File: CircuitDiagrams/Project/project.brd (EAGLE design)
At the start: 100 x 70 mm, 124 parts, among them IC1 UC3C, IC2 PCA9542A, IC3 MT48LC4M16A2TSOP54, IC4 TB6593FNGSSOP20, IC5 TB6593FNGSSOP20, J1 JTAG2.54MM2X5TH, J2 1BY2THROUGHHOLE, J3 1BY2THROUGHHOLE, J4 1BY2THROUGHHOLE, J5 8PIN2.54MM2X4TH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

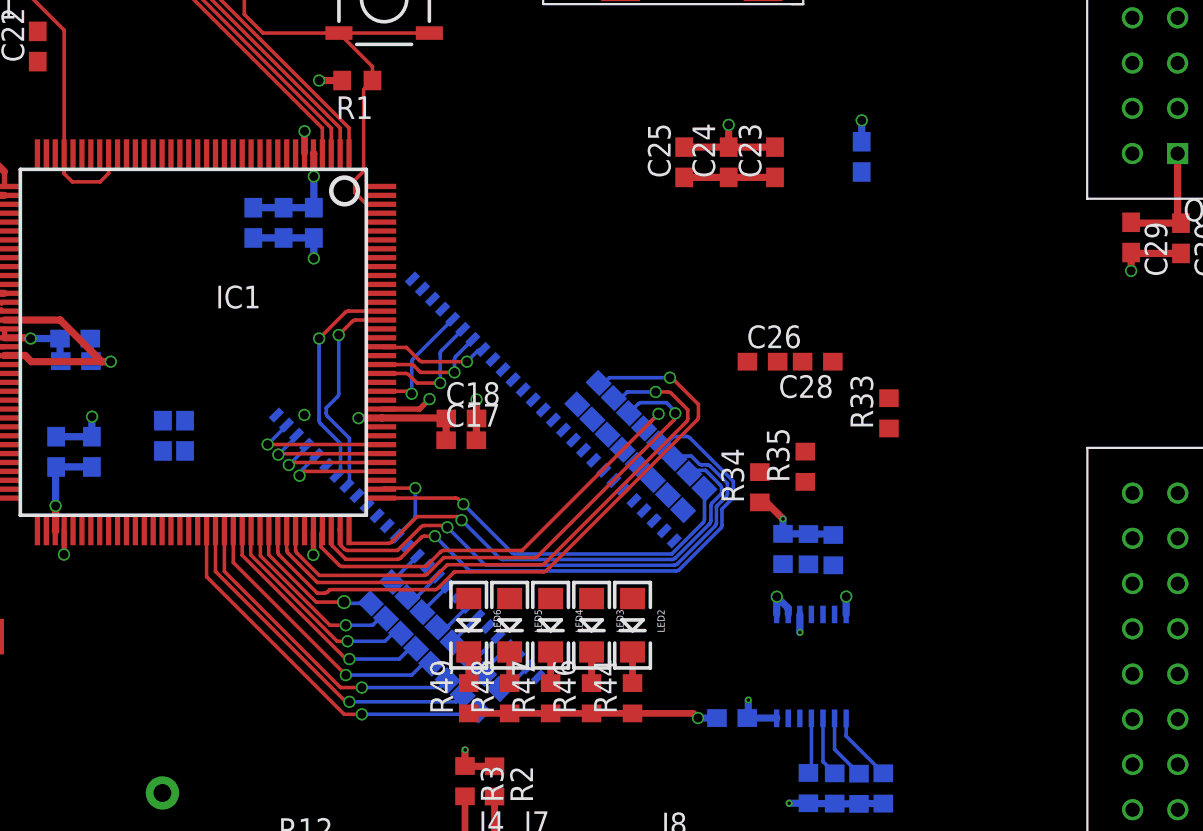
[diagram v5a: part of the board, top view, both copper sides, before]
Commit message: Routed the SDRAM
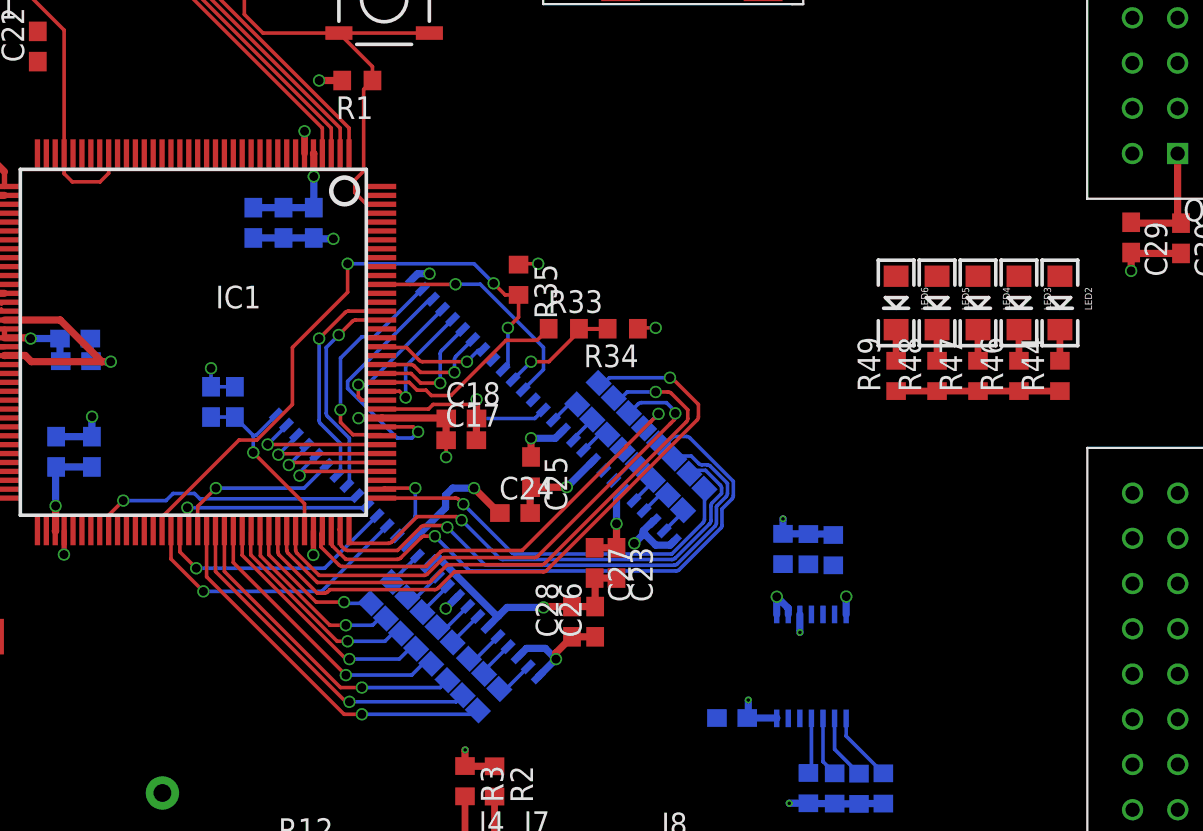
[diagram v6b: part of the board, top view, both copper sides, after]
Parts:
- moved LED2 30.1 mm to (90.4, 36.6)
- moved LED3 30.1 mm to (88.1, 36.6)
- moved LED4 30.1 mm to (85.8, 36.6)
- moved LED5 30.1 mm to (83.5, 36.6)
- moved LED6 30.1 mm to (81.2, 36.6)
- moved R44 30.1 mm to (90.4, 32.5)
- moved R46 30.1 mm to (88.1, 32.5)
- moved R47 30.1 mm to (85.8, 32.5)
- moved R48 30.1 mm to (83.5, 32.5)
- moved R49 30.1 mm to (81.2, 32.5)
- moved C27 27.3 mm to (64.3, 22.0), flipped to the top, turned to 270 degrees
- moved C23 24.2 mm to (65.5, 22.0), turned to 270 degrees
- moved C24 23.1 mm to (59.8, 24.8), turned to 0 degrees
- moved C28 20.1 mm to (63.0, 18.7), turned to 90 degrees
- moved C25 19.4 mm to (60.7, 27.1), turned to 270 degrees
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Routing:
- net PC14: track 0.00 -> 34.8 mm, vias 0 -> 3
- net +3V3: track 133.0 -> 162.5 mm, vias 23 -> 31
- net GND: track 157.5 -> 182.3 mm, vias 33 -> 34
- net PC15: track 0.00 -> 16.0 mm, vias 0 -> 1
- net PC8: track 0.00 -> 15.5 mm, vias 0 -> 1
- net PD10: track 0.00 -> 14.5 mm, vias 0 -> 1
- net PC16: track 0.00 -> 13.8 mm, vias 0 -> 1
- net PD24: track 0.00 -> 13.4 mm, vias 0 -> 1
- net PD9: track 0.00 -> 12.5 mm, vias 0 -> 1
- net PC17: track 0.00 -> 11.5 mm, vias 0 -> 1
- net PD13: track 0.00 -> 11.2 mm
- net PC18: track 0.00 -> 9.59 mm, vias 0 -> 1
- net PD11: track 0.00 -> 8.57 mm, vias 0 -> 1
- net SDRAMCLK: track 0.00 -> 8.11 mm, vias 0 -> 1
- net DQ08: track 0.00 -> 1.71 mm
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
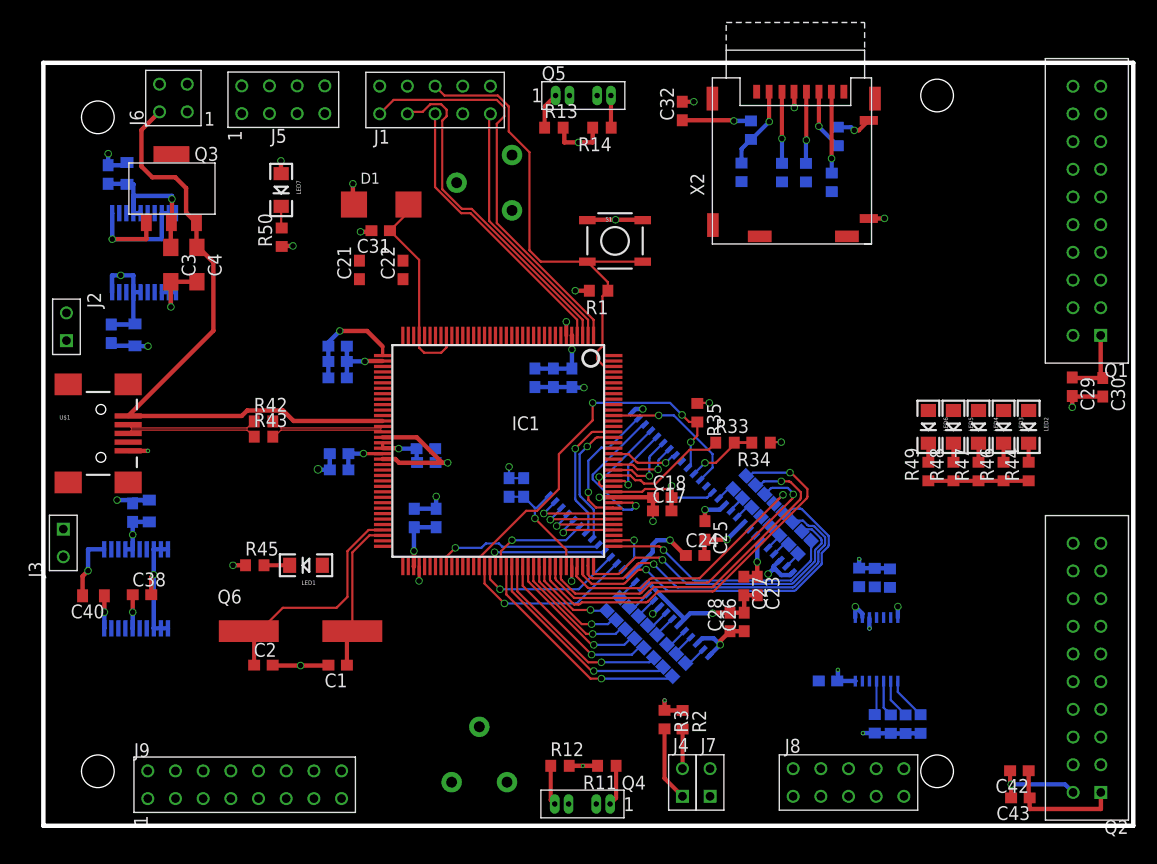
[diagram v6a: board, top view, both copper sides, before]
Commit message: Routed Camera Data Bus
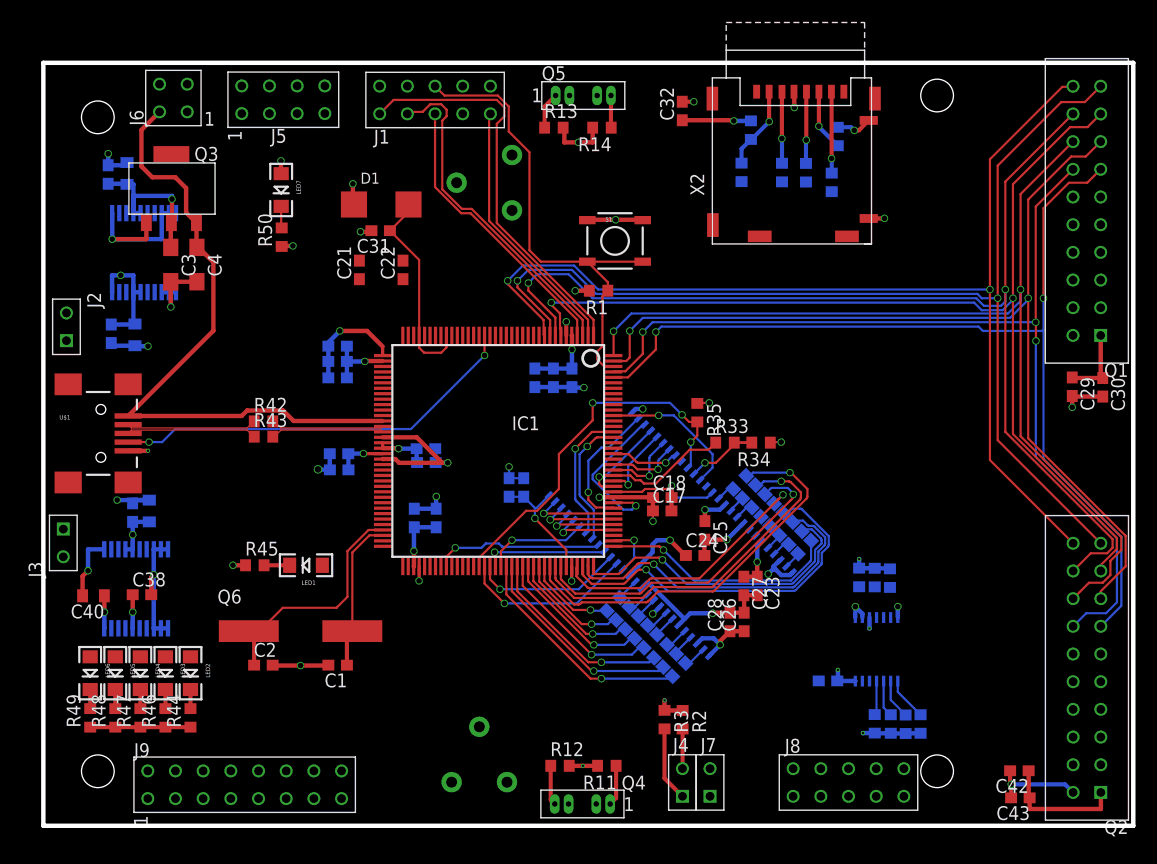
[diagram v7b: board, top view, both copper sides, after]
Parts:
- moved LED2 80.2 mm to (13.5, 14.0)
- moved LED5 80.2 mm to (6.60, 14.0)
- moved LED6 80.2 mm to (4.30, 14.0)
- moved R44 80.2 mm to (13.5, 9.90)
- moved R48 80.2 mm to (6.60, 9.90)
- moved R49 80.2 mm to (4.30, 9.90)
- moved LED3 80.2 mm to (11.2, 14.0)
- moved LED4 80.2 mm to (8.90, 14.0)
- moved R46 80.2 mm to (11.2, 9.90)
- moved R47 80.2 mm to (8.90, 9.90)
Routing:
- net PB5: track 0.00 -> 103.4 mm, vias 0 -> 2
- net PB6: track 0.00 -> 102.8 mm, vias 0 -> 2
- net PB7: track 0.00 -> 100.9 mm, vias 0 -> 2
- net PB4: track 0.00 -> 97.3 mm, vias 0 -> 2
- net PB3: track 0.00 -> 92.1 mm, vias 0 -> 2
- net PB2: track 0.00 -> 92.0 mm, vias 0 -> 2
- net PB0: track 0.00 -> 91.3 mm, vias 0 -> 2
- net PB1: track 0.00 -> 91.0 mm, vias 0 -> 3
- net PA4: track 0.00 -> 37.8 mm, vias 0 -> 2

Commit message: Routed Camera Control Lines
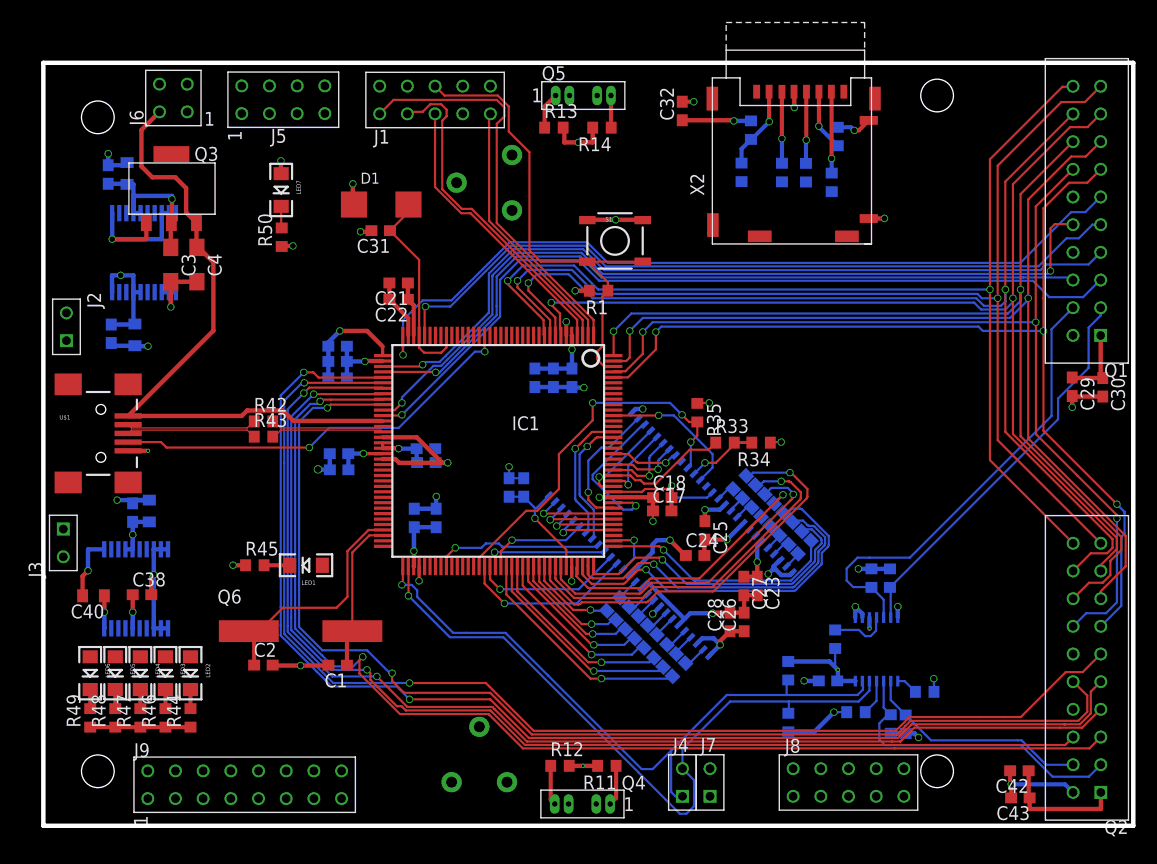
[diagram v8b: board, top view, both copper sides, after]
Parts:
- moved R3 12.2 mm to (68.3, 14.2), flipped to the bottom
- moved R2 9.70 mm to (68.4, 9.47), flipped to the bottom, turned to 90 degrees
- moved R10 6.08 mm to (72.6, 17.1), turned to 90 degrees
- moved C21 3.79 mm to (32.6, 49.8), turned to 180 degrees
- moved R5 2.97 mm to (80.9, 12.3), turned to 0 degrees
- moved C22 2.73 mm to (32.6, 48.3), turned to 180 degrees
- moved R4 2.03 mm to (74.6, 10.4), turned to 180 degrees
- moved R9 0.30 mm to (76.0, 22.7)
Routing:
- net PA22: track 0.00 -> 114.9 mm, vias 0 -> 2
- net PA23: track 0.00 -> 112.6 mm, vias 0 -> 2
- net PA24: track 0.00 -> 110.0 mm, vias 0 -> 2
- net PA26: track 0.00 -> 108.9 mm, vias 0 -> 2
- net PA27: track 0.00 -> 108.1 mm, vias 0 -> 2
- net PA25: track 0.00 -> 105.6 mm, vias 0 -> 2
- net PA28: track 0.00 -> 76.7 mm, vias 0 -> 2
- net PA29: track 0.00 -> 75.9 mm, vias 0 -> 1
- net PA19: track 0.00 -> 75.3 mm, vias 0 -> 1
- net PA20: track 0.00 -> 73.9 mm, vias 0 -> 1
- net PA21: track 0.00 -> 70.7 mm, vias 0 -> 1
- net PA15: track 0.00 -> 69.3 mm, vias 0 -> 1
- net PC3: track 3.64 -> 64.5 mm, vias 0 -> 1
- net PC2: track 6.87 -> 61.7 mm, vias 0 -> 1
- net SDA0: track 0.00 -> 42.2 mm
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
